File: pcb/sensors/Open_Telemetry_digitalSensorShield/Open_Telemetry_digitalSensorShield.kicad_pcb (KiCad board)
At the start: 4 copper layers, 50.8 x 22.9 mm, 45 parts, among them IC1 L80-M39, J1 73412-0110, J2 Conn_01x12_Female, J3 Conn_01x16_Female, Q1 BC846BPN, U1 BME280, U2 MPU-9250

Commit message: 2'nd internal review
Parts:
- removed @HOLE0, @HOLE1: , 
- removed D1: ASMB-MTB1-0A3A2, Open_Telemetry:AVAGO_PLCC4
- removed G***: LOGO, Open_Telemetry:BLUETOOTH
- removed G***: LOGO, Open_Telemetry:OpenFlyTelemetry
- removed G***: LOGO, Open_Telemetry:WIFI
- removed G***: LOGO, Open_Telemetry:GPS
- removed R17: 1k, RESC0603X26N
- removed U$31, U$32: MOUNTINGHOLE2.5, Adafruit HUZZAH32 ESP32 Feather:MOUNTINGHOLE_2.5_PLATED
- added LED3: , Open_Telemetry:AVAGO_PLCC4, F.Cu at (252.3, 148.4)
- C1, C2, C3, C4: footprint CAPC1608X87N -> Open_Telemetry:CAPC1608X87N
- C5: footprint CAPC1005X55N -> Open_Telemetry:CAPC1005X55N
- IC1: footprint L80-M39 -> Open_Telemetry:L80-M39
- J1: value 73412-0110 -> Ext GPS antenna connector
- J2: value Conn_01x12_Female -> PinHeader_01x12
- J3: value Conn_01x16_Female -> PinHeader_01x16
- LED1: value ExtAnt -> EXT ANT
- R1, R9: footprint RESC0603X26N -> Open_Telemetry:RESC0603X26N
- R10: value 10k -> 62; footprint RESC0603X26N -> Open_Telemetry:RESC1005X40N
- R11, R12, R13: value 1k -> 62; footprint RESC0603X26N -> Open_Telemetry:RESC1005X40N
- R14: value 1k -> 130; footprint RESC0603X26N -> Open_Telemetry:RESC1005X40N
- R15, R16: value 1k -> 10k; footprint RESC0603X26N -> Open_Telemetry:RESC0603X26N
- R2: value 10k -> 1k; footprint RESC0603X26N -> Open_Telemetry:RESC0603X26N
- R3: value 1k -> 100k; footprint RESC0603X26N -> Open_Telemetry:RESC0603X26N
- R4: value 100k -> NULL
- R5: value NULL -> 100k; footprint RESC0603X26N -> Open_Telemetry:RESC0603X26N
- R6: value 100k -> 1k; footprint RESC0603X26N -> Open_Telemetry:RESC0603X26N
- R7: value 1k -> NULL
- R8: value NULL -> 10k
- moved R16 17.2 mm to (245.5, 151.1)
- moved R10 9.30 mm to (252.4, 137.2)
- moved R15 8.81 mm to (257.8, 143.5), turned to 90 degrees
- moved R11 8.42 mm to (251.2, 144.1), turned to 270 degrees
- moved R14 6.68 mm to (248.6, 146.4)
- moved R5 3.92 mm to (245.5, 146.8), turned to 0 degrees
- moved R3 3.84 mm to (245.5, 144.8)
- moved R9 3.03 mm to (250.8, 135.4), turned to 0 degrees
- moved R7 2.67 mm to (245.5, 142.8)
- moved C7 1.69 mm to (242.6, 137.3)
- moved R4 1.38 mm to (245.5, 148.9)
- moved R13 1.26 mm to (252.3, 151.7)
- moved R12 1.22 mm to (248.4, 135.6)
- moved C3 0.97 mm to (240.0, 141.2)
- moved U1 0.92 mm to (248.5, 148.7), turned to 0 degrees
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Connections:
- IC1 pad 7: Net-(IC1-Pad7) -> (no net)
- IC1 pad 9: Net-(IC1-Pad9) -> (no net)
- J2 pad 1: Net-(J2-Pad1) -> (no net)
- J2 pad 10: Net-(J2-Pad10) -> (no net)
- J2 pad 2: Net-(J2-Pad2) -> (no net)
- J2 pad 3: Net-(J2-Pad3) -> (no net)
- J2 pad 7: Net-(J2-Pad7) -> (no net)
- J2 pad 8: Net-(J2-Pad8) -> (no net)
- J2 pad 9: Net-(J2-Pad9) -> (no net)
- J3 pad 10: UART_1_CLIENT_TXD -> (no net)
- J3 pad 11: Net-(J3-Pad11) -> (no net)
- J3 pad 12: Net-(J3-Pad12) -> (no net)
- J3 pad 14: Net-(J3-Pad14) -> (no net)
- J3 pad 4: Net-(J3-Pad4) -> (no net)
- J3 pad 5: Net-(J3-Pad5) -> (no net)
- J3 pad 6: Net-(J3-Pad6) -> (no net)
- J3 pad 8: Net-(J3-Pad8) -> UART_1_CLIENT_RXD
- J3 pad 9: UART_1_CLIENT_RXD -> UART_1_CLIENT_TXD
- R10 pad 1: +3V3 -> EXT_ANT
- R10 pad 2: INT_0 -> Net-(LED1-Pad2)
- R11 pad 1: EXT_ANT -> SAT_LOCK
- R11 pad 2: Net-(LED1-Pad2) -> Net-(LED2-Pad2)
- R12 pad 1: SAT_LOCK -> BLUE_LED
- R12 pad 2: Net-(LED2-Pad2) -> Net-(LED3-Pad3)
- R13 pad 1: BLUE_LED -> GREEN_LED
- R14 pad 1: GREEN_LED -> RED_LED
- R15 pad 1: RED_LED -> +3V3
- R15 pad 2: Net-(D1-Pad1) -> RESET
- R16 pad 1: Net-(R16-Pad1) -> +3V3
- R16 pad 2: GND -> CALIB
- R2 pad 1: Net-(R2-Pad1) -> Net-(IC1-Pad6)
- R2 pad 2: +3V3 -> Net-(Q1-Pad2)
- R3 pad 1: Net-(IC1-Pad6) -> GND
- R4 pad 2: Net-(Q1-Pad2) -> Net-(R1-Pad2)
- R5 pad 1: Net-(R1-Pad2) -> +3V3
- R5 pad 2: GND -> Net-(Q1-Pad5)
- R6 pad 1: +3V3 -> Net-(IC1-Pad8)
- R7 pad 1: Net-(IC1-Pad8) -> +3V3
- R7 pad 2: Net-(Q1-Pad5) -> Net-(R7-Pad2)
- R8 pad 1: +3V3 -> Net-(R7-Pad2)
- R8 pad 2: Net-(R8-Pad2) -> GND
- R9 pad 1: Net-(R8-Pad2) -> +3V3
- R9 pad 2: GND -> INT_0
- S1 pad 2: Net-(R16-Pad1) -> GND
- S2 pad 2: Net-(R17-Pad1) -> GND
- U1 pad 2: Net-(R2-Pad1) -> +3V3
- U2 pad 21: Net-(U2-Pad21) -> (no net)
- U2 pad 7: Net-(U2-Pad7) -> (no net)
- U2 pad 9: Net-(R8-Pad2) -> Net-(R7-Pad2)
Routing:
- net GND: track 86.3 -> 169.1 mm, vias 21 -> 28
- net Net-(IC1-Pad6): track 51.4 -> 11.3 mm
- net BLUE_LED: track 26.1 -> 8.34 mm
- net Net-(LED3-Pad3): track 0.00 -> 17.1 mm, vias 0 -> 2
- net Net-(R8-Pad2): track 13.2 -> 0.00 mm
- net Net-(LED2-Pad2): track 13.6 -> 1.88 mm
- net Net-(R17-Pad1): track 9.22 -> 0.00 mm
- net +3V3: track 34.3 -> 43.4 mm, vias 15 -> 14
- net RED_LED: track 41.5 -> 32.9 mm
- net SAT_LOCK: track 12.4 -> 4.00 mm, vias 2 -> 0
- net INT_0: track 22.6 -> 30.6 mm
- net Net-(R7-Pad2): track 0.00 -> 7.60 mm
- net Net-(R2-Pad1): track 7.30 -> 0.00 mm, vias 2 -> 0
- net Net-(D1-Pad1): track 6.58 -> 0.00 mm
- net (no net): track 0.00 -> 6.39 mm
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- added copper zone on B.Cu, net GND
- added copper zone on F.Cu, net GND
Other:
- board text added: "Coplanar wawe guide @ 1.5 GHz: Z =(Nom, Max, Min): 49.3 Ohm, X,Y Attenuation (Nom):<2 mdB , H: 0.11 mm (+/- 10%) T: 0.035 mm (+/- 10%) W: 1.4 mm (+/- 10%) S: 0.16 mm (+/- 10%) L: 2 mm (See https://www.pcbway.com/blog/Engineering_Technical/stackup___pcbway.html)"
- board text added: "KeepOut Signals"
- board text removed: "Z=50 Ohms @ 1.5 GHz"

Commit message: OFT001v1 Inertial HW board ready for internal review. Find it underpcb/sensors/Open_Telemetry_digitalSensorShield/...
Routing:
- net GND: track 169.1 -> 206.7 mm
- net (no net): track 6.39 -> 0.00 mm
- net Net-(IC1-Pad11): track 4.20 -> 3.12 mm
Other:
- board text added: "External GPS Antenna: Coplanar wawe guide @ 1.5 GHz: Z =(Nom, Max, Min): 49.9-, 59.5-, 41.5 Ohm Attenuation: <10 mdB Er 4.5 F/m (+/- 10%) H: 0.11 mm (+/- 10%) T: 0.035 mm (+/- 10%) W: 0.2 mm (+/- 10%) S: 0.16 mm (+/- 10%) L: 2 mm (See https://www.pcbway.com/blog/Engineering_Technical/stackup___pcbway.html)"
- board text removed: "Coplanar wawe guide @ 1.5 GHz: Z =(Nom, Max, Min): 49.3 Ohm, X,Y Attenuation (Nom):<2 mdB , H: 0.11 mm (+/- 10%) T: 0.035 mm (+/- 10%) W: 1.4 mm (+/- 10%) S: 0.16 mm (+/- 10%) L: 2 mm (See https://www.pcbway.com/blog/Engineering_Technical/stackup___pcbway.html)"

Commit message: First candidate for prototype manufacturing of OFT001 P1A01 sent to PCBWay after a early feedback. Close to manufacturing goahead.
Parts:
- added P1: MountingHole_2.5mm, MountingHole:MountingHole_2.5mm, F.Cu at (216.5, 134.5)
- added P2: MountingHole_2.5mm, MountingHole:MountingHole_2.5mm, F.Cu at (216.5, 152.3)
- added P3: MountingHole_2.2mm_M2, MountingHole:MountingHole_2.2mm_M2, F.Cu at (262.3, 133.9)
- added P4: MountingHole_2.2mm_M2, MountingHole:MountingHole_2.2mm_M2, F.Cu at (262.2, 152.9)
- LED3: value (none) -> Stat
- R8: footprint RESC0603X26N -> Open_Telemetry:RESC0603X26N
- S1, S2: footprint Open_Telemetry:ATS2D1G -> Open_Telemetry:KSR
- moved S1 0.39 mm to (256.2, 138.9)
- moved S2 0.13 mm to (256.2, 147.8)
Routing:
- net GND: track 206.7 -> 203.7 mm, vias 28 -> 29
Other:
- board text added: "Board SKU: OFT001v1 Designation name: Inertial navigation board v1 Version: P1A"
- board text added: "a,g"
- board text added: "m"
- board text added: "x"
- board text added: "y"
- board text added: "z"
- board text removed: "Board SKU: OFT001V1 Designation name: Inertial fusion V1 Version: P1A"

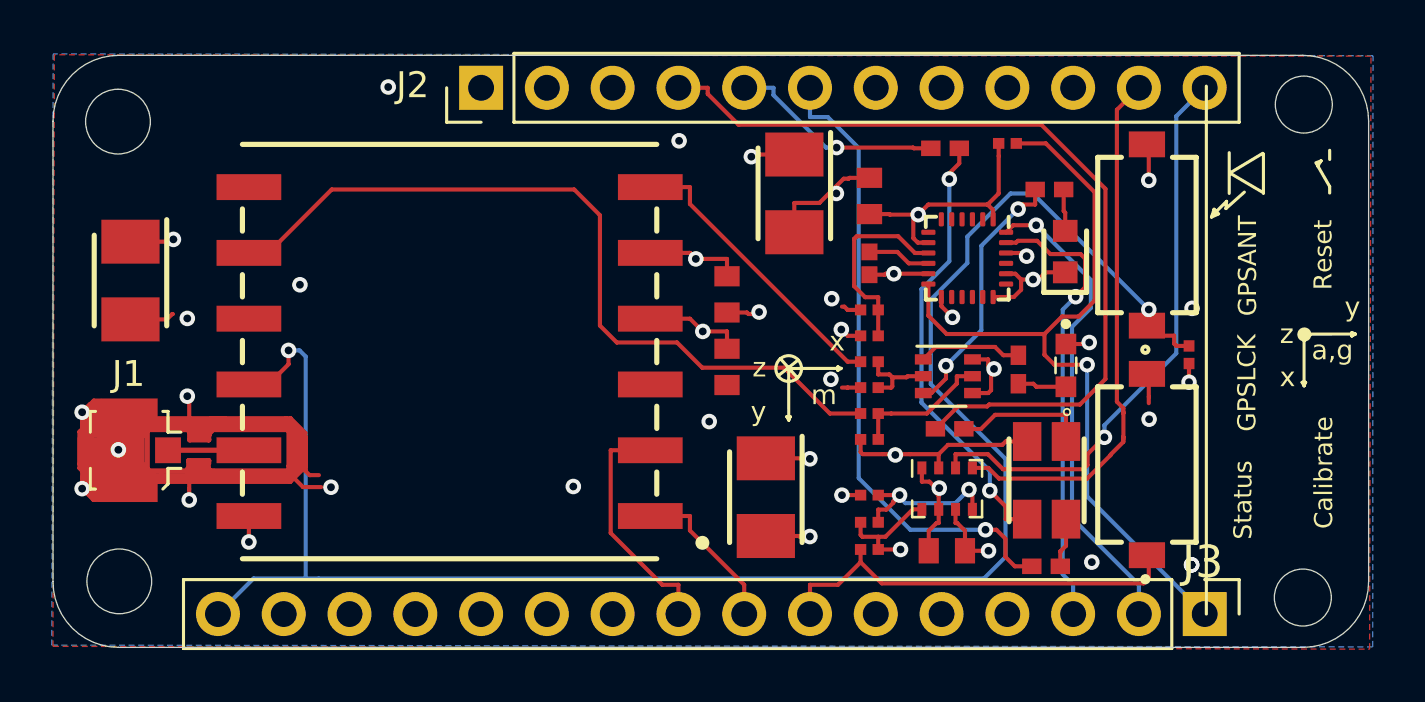
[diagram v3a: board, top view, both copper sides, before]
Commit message: P1A02 files sent to manufactuing review. Added R17, R18, R19, RR20 I2C pullups for reliability and hiher speeds.
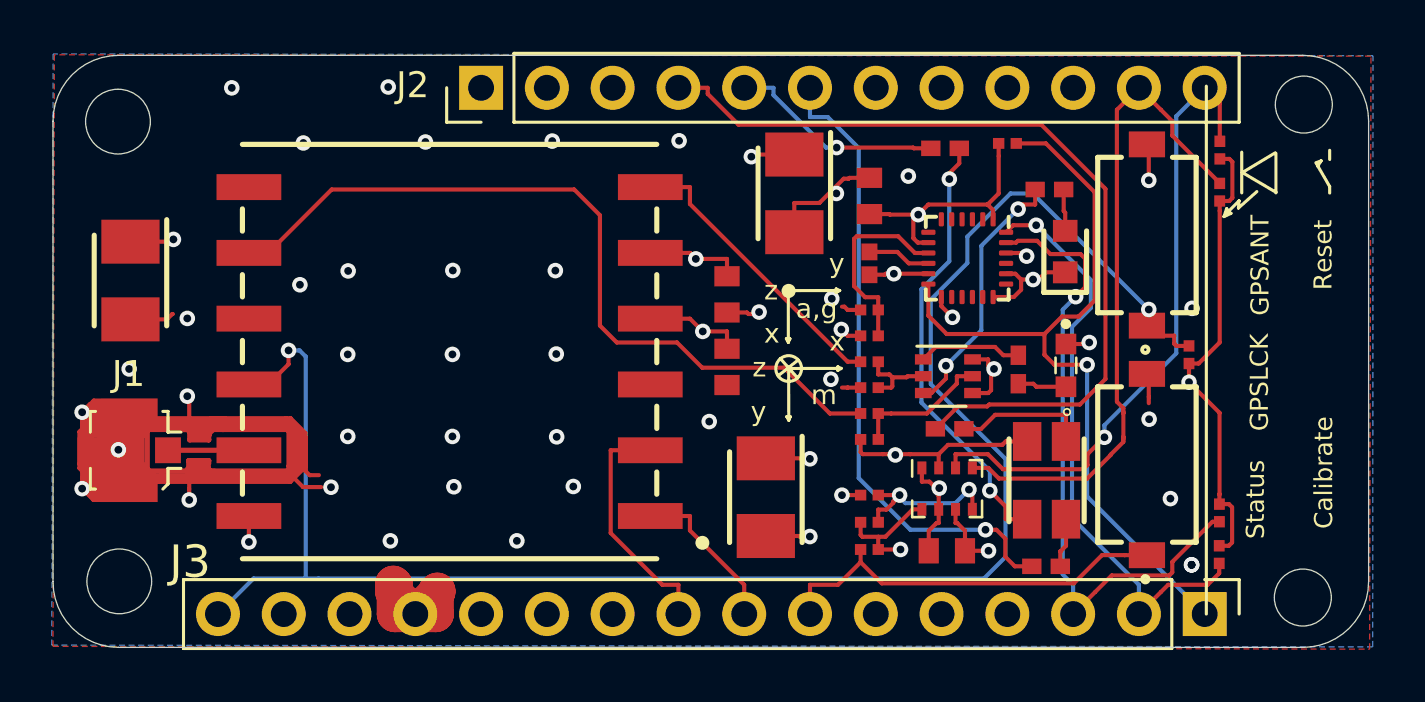
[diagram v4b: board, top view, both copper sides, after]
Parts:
- added R17: 10k, Open_Telemetry:RESC0603X26N, F.Cu at (259.0, 135.6)
- added R18: 10k, Open_Telemetry:RESC0603X26N, F.Cu at (259.0, 137.3)
- added R19: 1k, Open_Telemetry:RESC0603X26N, F.Cu at (259.0, 151.2)
- added R20: 1k, Open_Telemetry:RESC0603X26N, F.Cu at (259.0, 149.6)
- LED3: value Stat -> System Status
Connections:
- IC1 pad 7: (no net) -> Net-(IC1-Pad7)
- IC1 pad 9: (no net) -> Net-(IC1-Pad9)
- J2 pad 1: (no net) -> Net-(J2-Pad1)
- J2 pad 10: (no net) -> Net-(J2-Pad10)
- J2 pad 2: (no net) -> Net-(J2-Pad2)
- J2 pad 3: (no net) -> Net-(J2-Pad3)
- J2 pad 7: (no net) -> Net-(J2-Pad7)
- J2 pad 8: (no net) -> Net-(J2-Pad8)
- J2 pad 9: (no net) -> Net-(J2-Pad9)
- J3 pad 10: (no net) -> Net-(J3-Pad10)
- J3 pad 11: (no net) -> Net-(J3-Pad11)
- J3 pad 12: (no net) -> Net-(J3-Pad12)
- J3 pad 14: (no net) -> Net-(J3-Pad14)
- J3 pad 4: (no net) -> Net-(J3-Pad4)
- J3 pad 5: (no net) -> Net-(J3-Pad5)
- J3 pad 6: (no net) -> Net-(J3-Pad6)
- U2 pad 21: (no net) -> Net-(U2-Pad21)
- U2 pad 7: (no net) -> Net-(U2-Pad7)
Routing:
- net +3V3: track 43.4 -> 67.3 mm
- net GND: track 203.7 -> 213.6 mm, vias 29 -> 47
- net I2C_1_SCL_3V: track 17.6 -> 25.0 mm
- net I2C_0_SCL_3V: track 20.9 -> 25.9 mm
- net I2C_1_SDA_3V: track 18.5 -> 22.7 mm
- net I2C_0_SDA_3V: track 22.4 -> 24.7 mm
